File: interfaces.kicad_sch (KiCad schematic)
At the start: 66 parts, among them J12 USB C, J13 Tape In/Out, J3 Audio, U22 LM311, U23 LM1117MP-3.3, U24 LM1117MP-1.2, U26 ESP-12E, U27 LM1117MP-3.3, U6 SAM2695, U7 PCM1808PWR

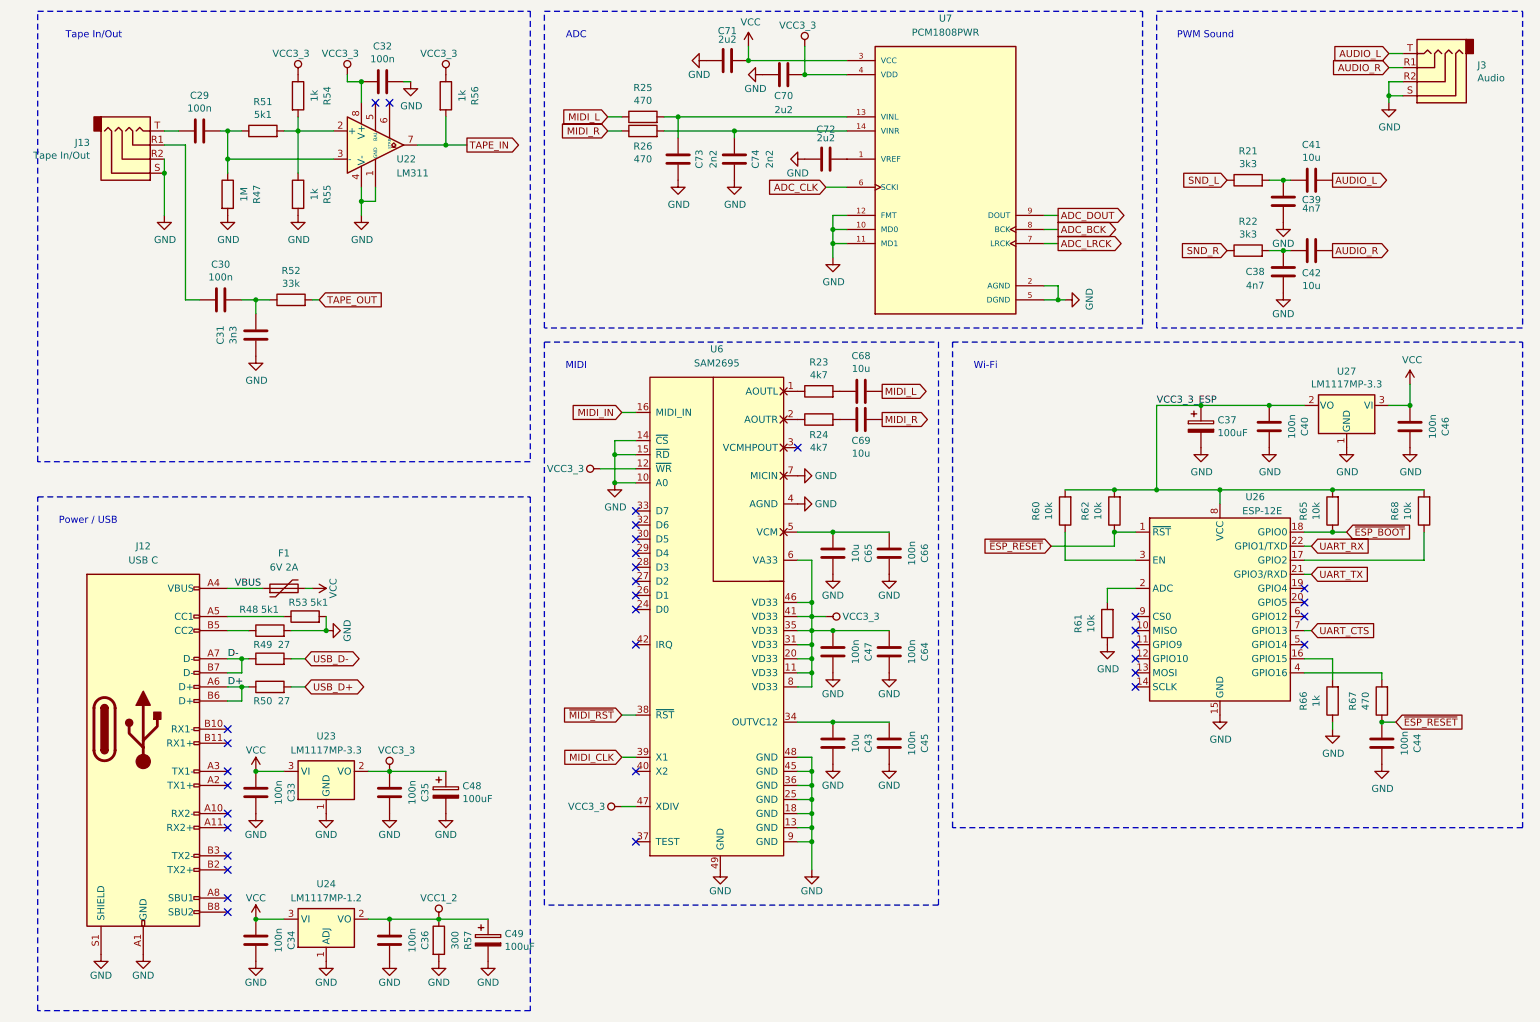
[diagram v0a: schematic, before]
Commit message: Updated revA: replaced resistors with IC for HDMI protection
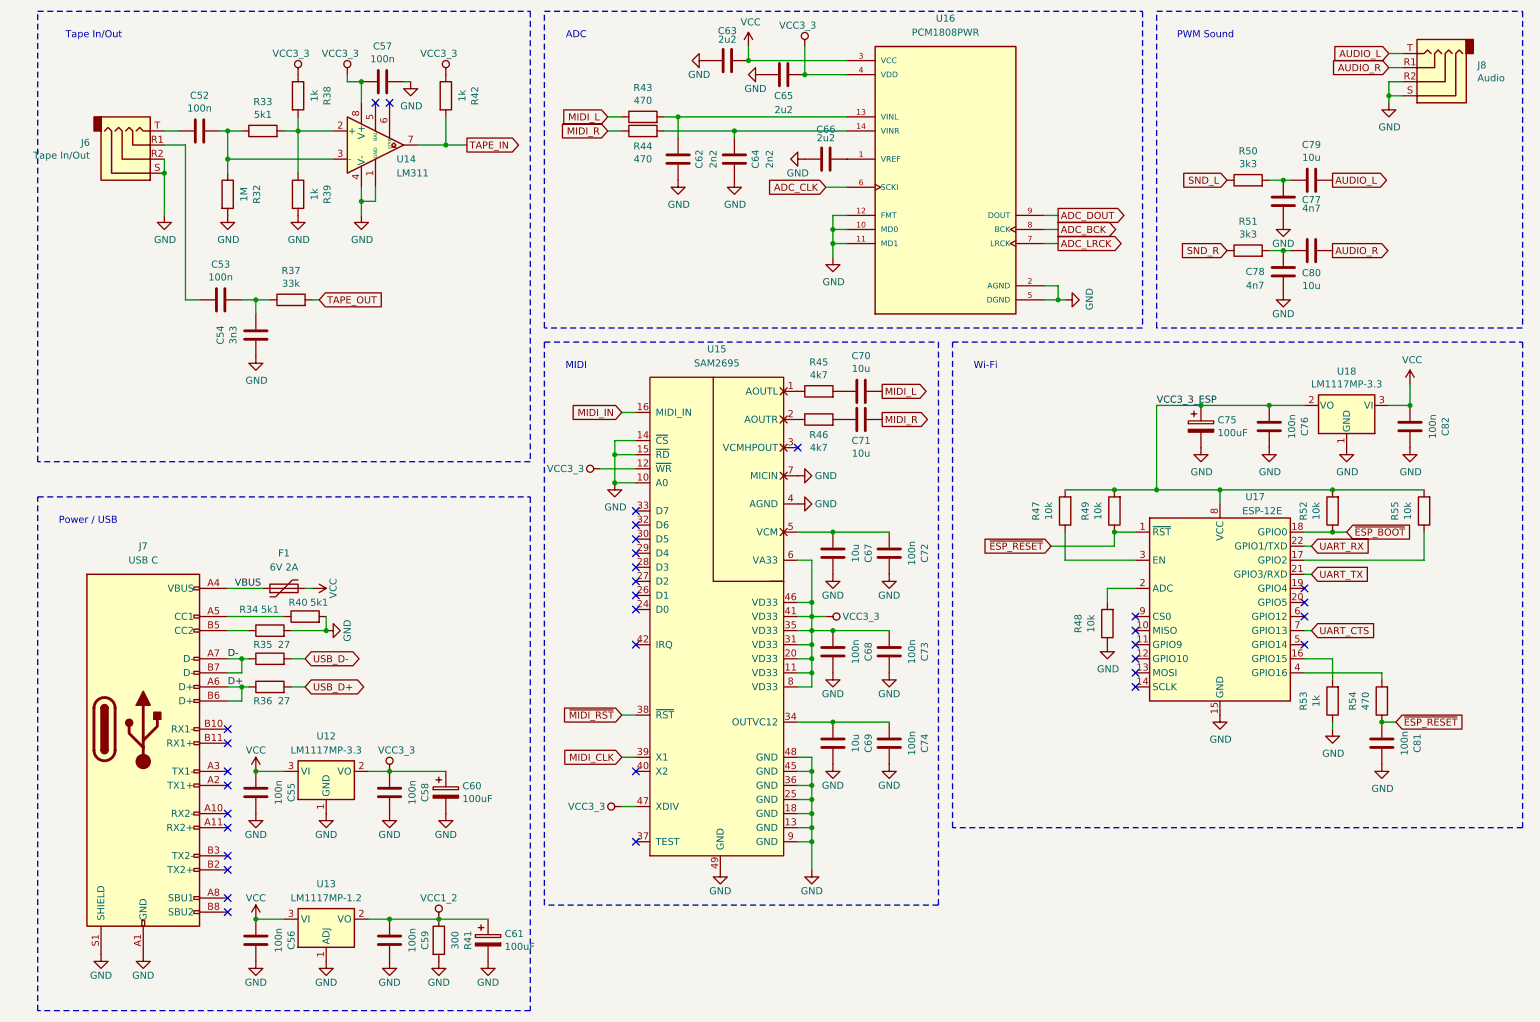
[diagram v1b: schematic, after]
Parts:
- renumbered C29 to C52, C30 to C53, C31 to C54, C33 to C55, C34 to C56, C32 to C57, C35 to C58, C36 to C59, C48 to C60, C49 to C61, C73 to C62, C71 to C63, C74 to C64, C70 to C65, C72 to C66, C65 to C67, C47 to C68, C43 to C69, C68 to C70, C69 to C71, C66 to C72, C64 to C73, C45 to C74, C37 to C75, C40 to C76, C39 to C77, C38 to C78, C41 to C79, C42 to C80, C44 to C81, C46 to C82, J13 to J6, J12 to J7, J3 to J8, R47 to R32, R51 to R33, R48 to R34, R49 to R35, R50 to R36, R52 to R37, R54 to R38, R55 to R39, R53 to R40, R57 to R41, R56 to R42, R25 to R43, R26 to R44, R23 to R45, R24 to R46, R60 to R47, R61 to R48, R62 to R49, R21 to R50, R22 to R51, R65 to R52, R66 to R53, R67 to R54, R68 to R55, U23 to U12, U24 to U13, U22 to U14, U6 to U15, U7 to U16, U26 to U17, U27 to U18

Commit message: Updated revB
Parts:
- added J10: Audio, Connector_PinHeader_1.27mm:PinHeader_1x03_P1.27mm_Vertical, symbol Connector_Generic:Conn_01x03
- added J9: 5V, Connector_PinHeader_1.27mm:PinHeader_1x02_P1.27mm_Vertical, symbol Connector_Generic:Conn_01x02
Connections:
- net AUDIO_L: now also J10.1 (Pin_1)
- net AUDIO_R: now also J10.3 (Pin_3)
- net GND: now also J10.2 (Pin_2), J9.2 (Pin_2)
- net VCC: now also J9.1 (Pin_1)
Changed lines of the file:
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@@
   (title_block
     (title "Karabas-Mini")
-    (date "2024-02-20")
-    (rev "A")
+    (date "2024-02-23")
+    (rev "B")
   )
   (junction (at 153.67 127) (diameter 0) (color 0 0 0 0)
@@
   (no_connect (at 151.13 93.98))
   (no_connect (at 212.09 132.08))
+  (wire (pts (xy 229.87 27.94) (xy 232.41 27.94))
+    (stroke (width 0) (type default))
+  )
   (wire (pts (xy 59.69 132.08) (xy 62.23 132.08))
     (stroke (width 0) (type default))
@@
     (stroke (width 0) (type default))
   )
+  (wire (pts (xy 229.87 30.48) (xy 232.41 30.48))
+    (stroke (width 0) (type default))
+  )
   (wire (pts (xy 199.39 67.31) (xy 198.12 67.31))
     (stroke (width 0) (type default))
@@
     (stroke (width 0) (type default))
   )
+  (wire (pts (xy 73.66 111.76) (xy 76.2 111.76))
+    (stroke (width 0) (type default))
+  )
   (wire (pts (xy 198.12 64.77) (xy 198.12 67.31))
     (stroke (width 0) (type default))
@@
     (stroke (width 0) (type default))
   )
+  (wire (pts (xy 229.87 33.02) (xy 232.41 33.02))
+    (stroke (width 0) (type default))
+  )
   (wire (pts (xy 73.66 179.07) (xy 77.47 179.07))
     (stroke (width 0) (type default))
@@
     (stroke (width 0) (type default))
   )
+  (wire (pts (xy 73.66 109.22) (xy 76.2 109.22))
+    (stroke (width 0) (type default))
+  )
   (wire (pts (xy 157.48 54.61) (xy 157.48 57.15))
     (stroke (width 0) (type default))
@@
     )
   )
+  (global_label "AUDIO_L" (shape input) (at 229.87 27.94 180) (fields_autoplaced)
+    (effects (font (size 1.27 1.27)) (justify right))
+    (property "Intersheetrefs" "${INTERSHEET_REFS}" (at 219.2647 27.94 0)
+      (effects (font (size 1.27 1.27)) (justify right) hide)
+    )
+  )
   (global_label "MIDI_IN" (shape input) (at 119.38 87.63 180) (fields_autoplaced)
     (effects (font (size 1.27 1.27)) (justify right))
@@
     )
   )
+  (global_label "AUDIO_R" (shape input) (at 229.87 33.02 180) (fields_autoplaced)
+    (effects (font (size 1.27 1.27)) (justify right))
+    (property "Intersheetrefs" "${INTERSHEET_REFS}" (at 219.0228 33.02 0)
+      (effects (font (size 1.27 1.27)) (justify right) hide)
+    )
+  )
   (global_label "ADC_LRCK" (shape output) (at 198.12 57.15 0) (fields_autoplaced)
     (effects (font (size 1.27 1.27)) (justify left))
@@
     )
   )
+  (symbol (lib_id "power:VCC") (at 73.66 109.22 90) (mirror x) (unit 1)
+    (in_bom yes) (on_board yes) (dnp no)
+    (property "Reference" "#PWR0189" (at 77.47 109.22 0)
+      (effects (font (size 1.27 1.27)) hide)
+    )
+    (property "Value" "VCC" (at 68.58 109.22 90)
+      (effects (font (size 1.27 1.27)))
+    )
+    (property "Footprint" "" (at 73.66 109.22 0)
+      (effects (font (size 1.27 1.27)) hide)
+    )
+    (property "Datasheet" "" (at 73.66 109.22 0)
+      (effects (font (size 1.27 1.27)) hide)
+    )
+    (pin "1")
+    (instances
+      (project "karabas-mini"
+        (path "/3ea0d469-753b-4b31-8a3d-1341413bdcc8/34157a6c-fe5b-4b27-a58b-efdaac9599d0"
+          (reference "#PWR0189") (unit 1)
+        )
+      )
+    )
+  )
   (symbol (lib_id "Device:C") (at 53.34 73.66 180) (unit 1)
     (in_bom yes) (on_board yes) (dnp no)
@@
     )
   )
+  (symbol (lib_id "Connector_Generic:Conn_01x02") (at 81.28 109.22 0) (unit 1)
+    (in_bom yes) (on_board yes) (dnp no) (fields_autoplaced)
+    (property "Reference" "J9" (at 83.82 109.22 0)
+      (effects (font (size 1.27 1.27)) (justify left))
+    )
+    (property "Value" "5V" (at 83.82 111.76 0)
+      (effects (font (size 1.27 1.27)) (justify left))
+    )
+    (property "Footprint" "Connector_PinHeader_1.27mm:PinHeader_1x02_P1.27mm_Vertical" (at 81.28 109.22 0)
+      (effects (font (size 1.27 1.27)) hide)
+    )
+    (property "Datasheet" "~" (at 81.28 109.22 0)
+      (effects (font (size 1.27 1.27)) hide)
+    )
+    (pin "1")
+    (pin "2")
+    (instances
+      (project "karabas-mini"
+        (path "/3ea0d469-753b-4b31-8a3d-1341413bdcc8/34157a6c-fe5b-4b27-a58b-efdaac9599d0"
+          (reference "J9") (unit 1)
+        )
+      )
+    )
+  )
+  (symbol (lib_id "power:GND") (at 73.66 111.76 270) (mirror x) (unit 1)
+    (in_bom yes) (on_board yes) (dnp no)
+    (property "Reference" "#PWR0190" (at 67.31 111.76 0)
+      (effects (font (size 1.27 1.27)) hide)
+    )
+    (property "Value" "GND" (at 68.58 111.76 90)
+      (effects (font (size 1.27 1.27)))
+    )
+    (property "Footprint" "" (at 73.66 111.76 0)
+      (effects (font (size 1.27 1.27)) hide)
+    )
+    (property "Datasheet" "" (at 73.66 111.76 0)
+      (effects (font (size 1.27 1.27)) hide)
+    )
+    (pin "1")
+    (instances
+      (project "karabas-mini"
+        (path "/3ea0d469-753b-4b31-8a3d-1341413bdcc8/34157a6c-fe5b-4b27-a58b-efdaac9599d0"
+          (reference "#PWR0190") (unit 1)
+        )
+      )
+    )
+  )
   (symbol (lib_id "power:GND") (at 207.01 129.54 0) (unit 1)
     (in_bom yes) (on_board yes) (dnp no)
@@
     )
   )
+  (symbol (lib_id "power:GND") (at 229.87 30.48 270) (mirror x) (unit 1)
+    (in_bom yes) (on_board yes) (dnp no)
+    (property "Reference" "#PWR0191" (at 223.52 30.48 0)
+      (effects (font (size 1.27 1.27)) hide)
+    )
+    (property "Value" "GND" (at 224.79 30.48 90)
+      (effects (font (size 1.27 1.27)))
+    )
+    (property "Footprint" "" (at 229.87 30.48 0)
+      (effects (font (size 1.27 1.27)) hide)
+    )
+    (property "Datasheet" "" (at 229.87 30.48 0)
+      (effects (font (size 1.27 1.27)) hide)
+    )
+    (pin "1")
+    (instances
+      (project "karabas-mini"
+        (path "/3ea0d469-753b-4b31-8a3d-1341413bdcc8/34157a6c-fe5b-4b27-a58b-efdaac9599d0"
+          (reference "#PWR0191") (unit 1)
+        )
+      )
+    )
+  )
   (symbol (lib_id "power:GND") (at 53.34 160.02 0) (unit 1)
     (in_bom yes) (on_board yes) (dnp no)
@@
         )
       )
+    )
+  )
+  (symbol (lib_id "Connector_Generic:Conn_01x03") (at 237.49 30.48 0) (unit 1)
+    (in_bom yes) (on_board yes) (dnp no) (fields_autoplaced)
+    (property "Reference" "J10" (at 240.03 29.21 0)
+      (effects (font (size 1.27 1.27)) (justify left))
+    )
+    (property "Value" "Audio" (at 240.03 31.75 0)
+      (effects (font (size 1.27 1.27)) (justify left))
+    )
+    (property "Footprint" "Connector_PinHeader_1.27mm:PinHeader_1x03_P1.27mm_Vertical" (at 237.49 30.48 0)
+      (effects (font (size 1.27 1.27)) hide)
+    )
+    (property "Datasheet" "~" (at 237.49 30.48 0)
+      (effects (font (size 1.27 1.27)) hide)
+    )
+    (pin "1")
+    (pin "3")
+    (pin "2")
+    (instances
+      (project "karabas-mini"
+        (path "/3ea0d469-753b-4b31-8a3d-1341413bdcc8/34157a6c-fe5b-4b27-a58b-efdaac9599d0"
+          (reference "J10") (unit 1)
+        )
+      )

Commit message: Small improvements revC
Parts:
- C66: value 2u2 -> 10u
- R45, R46: value 4k7 -> 1k
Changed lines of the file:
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@@
       (effects (font (size 1.27 1.27)))
     )
-    (property "Value" "4k7" (at 154.94 93.98 90)
+    (property "Value" "1k" (at 154.94 93.98 90)
       (effects (font (size 1.27 1.27)))
     )
@@
       (effects (font (size 1.27 1.27)))
     )
-    (property "Value" "4k7" (at 154.94 80.8736 90)
+    (property "Value" "1k" (at 154.94 80.8736 90)
       (effects (font (size 1.27 1.27)))
     )
@@
       (effects (font (size 1.27 1.27)))
     )
-    (property "Value" "2u2" (at 156.21 38.1 90)
-      (effects (font (size 1.27 1.27)))
-    )
+    (property "Value" "10u" (at 156.21 38.1 90)
+      (effects (font (size 1.27 1.27)))
+    )

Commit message: PCB revD
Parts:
- added R57, R58, R59: 27, Resistor_SMD:R_0603_1608Metric_Pad0.98x0.95mm_HandSolder, symbol Device:R
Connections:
- net ADC_BCK: now also R57.2; no longer U16.8 (BCK)
- net ADC_CLK: now also R59.1; no longer U16.6 (SCKI)
- net ADC_LRCK: now also R58.2; no longer U16.7 (LRCK)
- new net: R58.1, U16.7 (LRCK)
- new net: R59.2, U16.6 (SCKI)
- new net: R57.1, U16.8 (BCK)
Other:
- moved on the sheet: C77, C78, C79, C80, J10, R50, R51

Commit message: revF
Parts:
- removed J7: USB C, Connector_USB:USB_C_Receptacle_HCTL_HC-TYPE-C-16P-01A, symbol Connector:USB_C_Receptacle
- added J7: Molex 2169890001, TypeC:MOLEX_2169890001, symbol Molex TypeC:2169890001
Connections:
- net D+: now also J7.A6 (DA+), J7.B6 (DB+)
- net D-: now also J7.A7 (DA-), J7.B7 (DB-)
- net GND: now also R40.1, J7.A1 (GND1), J7.A12 (GND2), J7.B1 (GND3), J7.B12 (GND4), J7.SH1 (SHIELD1), J7.SH2 (SHIELD2), J7.SH3 (SHIELD3), J7.SH4 (SHIELD4); no longer R40.2
- net VBUS: now also J7.A4 (VBUS1), J7.A9 (VBUS2), J7.B4 (VBUS3), J7.B9 (VBUS4)
- net at R34.1: now also J7.B5 (CC2)
- new net: J7.A5 (CC1), R40.2
- no-connect marks 34 -> 24
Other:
- moved on the sheet: C55, C58, C60, F1, J9, R34, R35, R36, R40, U12

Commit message: revF3
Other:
- note added: "* rev F3 uses a chinese connector https://www.aliexpress.com/item/ 1005006199511838.html"
- note added: "* revF,F1,F2 uses Molex 2169890001"
- note added: "Alternatives: - Molex 2169890001 - Kycon KUSBX-SL-CS1N14-B - Amphenol 12402054M611A"
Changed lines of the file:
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@@
     (fill (type none))
+  )
+  (text "* revF,F1,F2 uses Molex 2169890001" (at 64.77 144.78 0)
+    (effects (font (size 1.27 1.27)) (justify left bottom))
   )
   (text "Power / USB" (at 16.51 193.04 0)
@@
     (effects (font (size 1.27 1.27)) (justify right bottom))
   )
+  (text "* rev F3 uses a chinese connector\nhttps://www.aliexpress.com/item/\n1005006199511838.html"
+    (at 64.77 151.13 0)
+    (effects (font (size 1.27 1.27)) (justify left bottom))
+  )
   (text "Tape In/Out" (at 29.21 20.32 0)
     (effects (font (size 1.27 1.27)) (justify right bottom))
@@
     (effects (font (size 1.27 1.27)) (justify right bottom))
   )
+  (text "Alternatives:\n- Molex 2169890001\n- Kycon KUSBX-SL-CS1N14-B\n- Amphenol 12402054M611A\n"
+    (at 67.31 139.7 0)
+    (effects (font (size 1.27 1.27)) (justify left bottom))
+  )
   (label "D-" (at 19.05 127 0) (fields_autoplaced)

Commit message: revG
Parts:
- removed J10: Audio, Connector_PinHeader_1.27mm:PinHeader_1x03_P1.27mm_Vertical, symbol Connector_Generic:Conn_01x03
- removed R50, R51: 3k3, Resistor_SMD:R_0603_1608Metric_Pad0.98x0.95mm_HandSolder, symbol Device:R
- added C40, C41: 10u, Capacitor_SMD:C_0603_1608Metric_Pad1.08x0.95mm_HandSolder, symbol Device:C
- added C92: 100n, Capacitor_SMD:C_0603_1608Metric_Pad1.08x0.95mm_HandSolder, symbol Device:C
- added C93, C94: 22pF, Capacitor_SMD:C_0603_1608Metric_Pad1.08x0.95mm_HandSolder, symbol Device:C
- added R71, R72: 220k, Resistor_SMD:R_0603_1608Metric_Pad0.98x0.95mm_HandSolder, symbol Device:R
- added R73, R90: 100, Resistor_SMD:R_0603_1608Metric_Pad0.98x0.95mm_HandSolder, symbol Device:R
- added U21: UDA1334ATS, Package_SO:SSOP-16_4.4x5.2mm_P0.65mm, symbol Audio:UDA1334ATS
- added Y3: 12MHz, Crystal:Crystal_SMD_3225-4Pin_3.2x2.5mm_HandSoldering, symbol Device:Crystal_GND24
- C77, C78: value 4n7 -> 100n
- C79: value 10u -> 100n
- J7: value Molex 2169890001 -> Type-C right angle "flag" type
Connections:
- net AUDIO_L: now also C77.1, R73.2; no longer C79.2
- net AUDIO_R: now also C78.1, R90.2; no longer C80.2
- net GND: now also C79.2, C80.2, C92.1, C93.2, C94.2, R71.1, R72.1, U21.10 (PLL0), U21.11 (SFOR0), U21.15 (VSSA), U21.5 (VSSD), U21.6 (SYSCLK/PLL1), U21.7 (SFOR1), U21.8 (MUTE), U21.9 (DEEM/CLKOUT), Y3.2, Y3.4
- net VCC3_3: now also C92.2, U21.13 (VDDA), U21.4 (VDDD)
- net at C79.1: now also C80.1, U21.12 (Vref(DAC)); no longer C77.1
- net MIDI_X2: now reaches U15.40 (X2)
- net MIDI_X2: now also C94.1, Y3.3
- net MIDI_CLK renamed MIDI_X1
- net MIDI_X1: now also C93.1, Y3.1
- net ~{ESP_BOOT}: no longer names the net of R52.1, U17.18 (GPIO0)
- new net: C40.2, R71.2, R73.1
- new net: C40.1, U21.14 (VOUTL)
- new net: C41.1, U21.16 (VOUTR)
- new net: C41.2, R72.2, R90.1
- new net DAC_BCK: U21.1 (BCK)
- new net DAC_DAT: U21.3 (DATAI)
- new net DAC_WS: U21.2 (WS)
- no-connect marks 24 -> 23
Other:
- note added: "DAC"
- note removed: "* rev F3 uses a chinese connector https://www.aliexpress.com/item/ 1005006199511838.html"
- note removed: "* revF,F1,F2 uses Molex 2169890001"
- note removed: "Alternatives: - Molex 2169890001 - Kycon KUSBX-SL-CS1N14-B - Amphenol 12402054M611A"
- note removed: "PWM Sound"
- moved on the sheet: C52, C53, C54, C57, C62, C63, C64, C65, C66, J6, J8, R32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
